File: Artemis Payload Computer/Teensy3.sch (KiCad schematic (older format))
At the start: 1 part

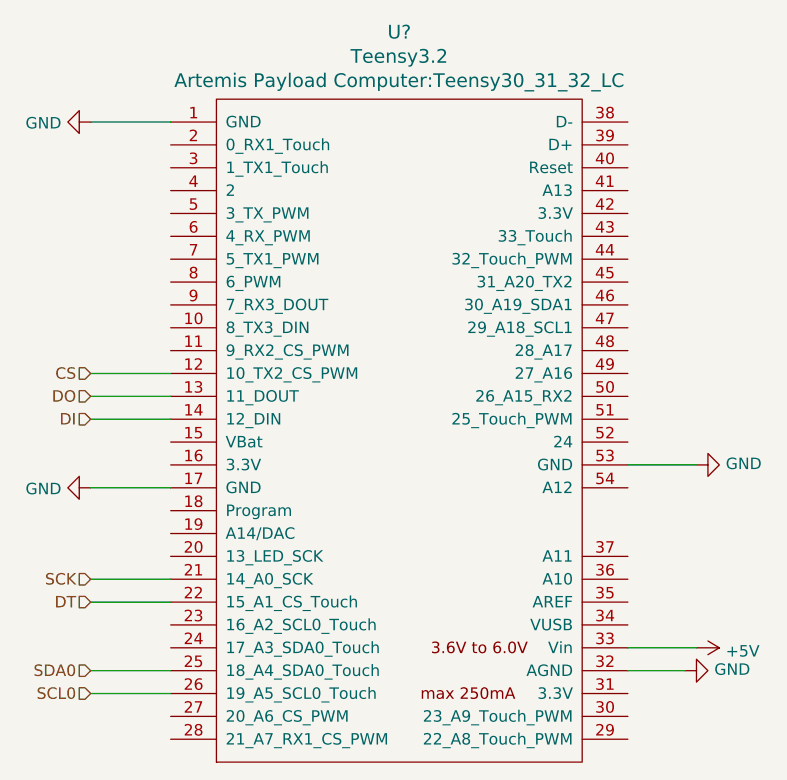
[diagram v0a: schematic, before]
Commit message: started tracing... they are bad
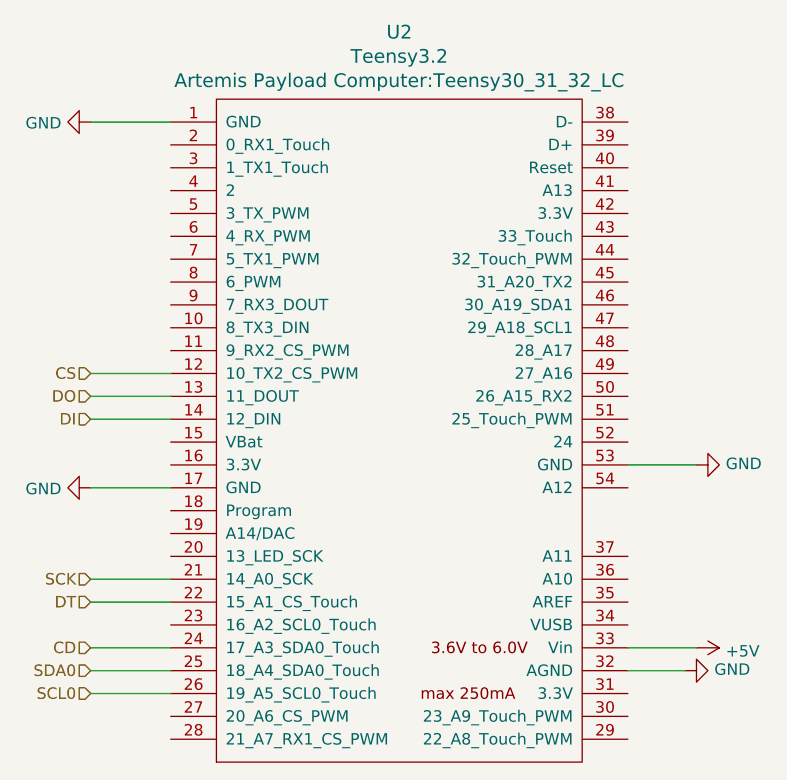
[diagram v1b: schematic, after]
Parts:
- gave numbers to parts that had none: 1
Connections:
- net CD: now reaches U2.24 (17_A3_SDA0_Touch)
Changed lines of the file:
@@
 $Descr A4 11693 8268
 encoding utf-8
-Sheet 3 7
+Sheet 7 7
 Title ""
 Date ""
@@
 $EndDescr
 $Comp
-L Artemis_Footprints:Teensy3.2 U?
+L Artemis_Footprints:Teensy3.2 U2
 U 1 1 6028516C
 P 6350 3600
-F 0 "U?" H 6350 5343 60  0000 C CNN
+F 0 "U2" H 6350 5343 60  0000 C CNN
 F 1 "Teensy3.2" H 6350 5237 60  0000 C CNN
 F 2 "Artemis Payload Computer:Teensy30_31_32_LC" H 6350 5131 60  0000 C CNN
@@
 $EndComp
 $Comp
-L power:GND #PWR?
+L power:GND #PWR0106
 U 1 1 60404CA5
 P 5000 2250
-F 0 "#PWR?" H 5000 2000 50  0001 C CNN
+F 0 "#PWR0106" H 5000 2000 50  0001 C CNN
 F 1 "GND" V 5005 2122 50  0000 R CNN
 F 2 "" H 5000 2250 50  0001 C CNN
@@
 $EndComp
 $Comp
-L power:GND #PWR?
+L power:GND #PWR0107
 U 1 1 604051D4
 P 5000 3850
-F 0 "#PWR?" H 5000 3600 50  0001 C CNN
+F 0 "#PWR0107" H 5000 3600 50  0001 C CNN
 F 1 "GND" V 5005 3722 50  0000 R CNN
 F 2 "" H 5000 3850 50  0001 C CNN
@@
 $EndComp
 $Comp
-L power:GND #PWR?
+L power:GND #PWR0108
 U 1 1 6040567B
 P 7600 4650
-F 0 "#PWR?" H 7600 4400 50  0001 C CNN
+F 0 "#PWR0108" H 7600 4400 50  0001 C CNN
 F 1 "GND" V 7605 4522 50  0000 R CNN
 F 2 "" H 7600 4650 50  0001 C CNN
@@
 	5350 4750 5000 4750
 $Comp
-L power:+5V #PWR?
+L power:+5V #PWR0117
 U 1 1 6047F910
 P 7650 4550
-F 0 "#PWR?" H 7650 4400 50  0001 C CNN
+F 0 "#PWR0117" H 7650 4400 50  0001 C CNN
 F 1 "+5V" V 7665 4678 50  0000 L CNN
 F 2 "" H 7650 4550 50  0001 C CNN
@@
 	7650 4550 7350 4550
 $Comp
-L power:GND #PWR?
+L power:GND #PWR0118
 U 1 1 6047FEAC
 P 7650 3750
-F 0 "#PWR?" H 7650 3500 50  0001 C CNN
+F 0 "#PWR0118" H 7650 3500 50  0001 C CNN
 F 1 "GND" V 7655 3622 50  0000 R CNN
 F 2 "" H 7650 3750 50  0001 C CNN
@@
 Wire Wire Line
 	5000 4350 5350 4350
+Text HLabel 5000 4550 0    50   Input ~ 0
+CD
+Wire Wire Line
+	5350 4550 5000 4550
 $EndSCHEMATC

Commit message: ready for review
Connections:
- no-connect marks 0 -> 1
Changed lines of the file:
@@
 Wire Wire Line
 	5350 4550 5000 4550
+NoConn ~ 7350 3650
 $EndSCHEMATC
